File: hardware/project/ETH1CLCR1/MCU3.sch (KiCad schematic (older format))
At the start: 19 parts, among them J1201 Conn_02x05, U1001 STM32F413RGT6Tx, U1202 24LC08B-E/MS, Y1201 NX3225GD-8MHZ-STD-CRA-3

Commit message: Schematic design
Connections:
- net +3.3VP renamed +3.3VF
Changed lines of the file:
@@
 $Descr A3 16535 11693
 encoding utf-8
-Sheet 10 14
+Sheet 9 16
 Title ""
 Date ""
@@
 Wire Wire Line
 	7400 3100 7500 3100
-$Comp
-L power:+3.3VP #PWR?
-U 1 1 5E29D79D
-P 7550 3050
-AR Path="/5DF36C25/5E29D79D" Ref="#PWR?"  Part="1"
-AR Path="/5E29C232/5E29D79D" Ref="#PWR01201"  Part="1"
-AR Path="/5DF38F82/5E29D79D" Ref="#PWR01001"  Part="1"
-F 0 "#PWR01001" H 7700 3000 50  0001 C CNN
-F 1 "+3.3VP" H 7570 3193 50  0000 C CNN
-F 2 "" H 7550 3050 50  0001 C CNN
-F 3 "" H 7550 3050 50  0001 C CNN
-	1    7550 3050
-	1    0    0    -1
-$EndComp
 Wire Wire Line
 	7550 3050 7550 3100
@@
 Connection ~ 9300 9800
 $Comp
-L power:+3.3VP #PWR01010
-U 1 1 5E770710
-P 9900 10050
-F 0 "#PWR01010" H 10050 10000 50  0001 C CNN
-F 1 "+3.3VP" H 9920 10193 50  0000 C CNN
-F 2 "" H 9900 10050 50  0001 C CNN
-F 3 "" H 9900 10050 50  0001 C CNN
-	1    9900 10050
-	1    0    0    -1
-$EndComp
-$Comp
 L ETH1CLCR1:DGNDF #PWR01014
 U 1 1 5E77122F
@@
 	1    0    0    -1
 $EndComp
-$Comp
-L power:+3.3VP #PWR01009
-U 1 1 5E7718B5
-P 8000 9950
-F 0 "#PWR01009" H 8150 9900 50  0001 C CNN
-F 1 "+3.3VP" H 8020 10093 50  0000 C CNN
-F 2 "" H 8000 9950 50  0001 C CNN
-F 3 "" H 8000 9950 50  0001 C CNN
-	1    8000 9950
-	1    0    0    -1
-$EndComp
 Wire Wire Line
 	8000 9950 8000 10000
-$Comp
-L power:+3.3VP #PWR01008
-U 1 1 5E772DFA
-P 9300 9750
-F 0 "#PWR01008" H 9450 9700 50  0001 C CNN
-F 1 "+3.3VP" H 9320 9893 50  0000 C CNN
-F 2 "" H 9300 9750 50  0001 C CNN
-F 3 "" H 9300 9750 50  0001 C CNN
-	1    9300 9750
-	1    0    0    -1
-$EndComp
 $Comp
 L Device:C C1003
@@
 F 3 "" H 14150 6300 50  0001 C CNN
 	1    14150 6300
-	1    0    0    -1
-$EndComp
-$Comp
-L power:+3.3VP #PWR01002
-U 1 1 5E7C0507
-P 14150 5600
-F 0 "#PWR01002" H 14300 5550 50  0001 C CNN
-F 1 "+3.3VP" H 14170 5743 50  0000 C CNN
-F 2 "" H 14150 5600 50  0001 C CNN
-F 3 "" H 14150 5600 50  0001 C CNN
-	1    14150 5600
 	1    0    0    -1
 $EndComp
@@
 Wire Wire Line
 	2200 10700 2450 10700
-$Comp
-L power:+3.3VP #PWR01011
-U 1 1 5E10E793
-P 2200 10250
-F 0 "#PWR01011" H 2350 10200 50  0001 C CNN
-F 1 "+3.3VP" H 2220 10393 50  0000 C CNN
-F 2 "" H 2200 10250 50  0001 C CNN
-F 3 "" H 2200 10250 50  0001 C CNN
-	1    2200 10250
-	1    0    0    -1
-$EndComp
 Wire Wire Line
 	2200 10250 2200 10300
@@
 $EndComp
 $Comp
-L power:+3.3VP #PWR01012
-U 1 1 5DEC5CD8
-P 4100 10250
-F 0 "#PWR01012" H 4250 10200 50  0001 C CNN
-F 1 "+3.3VP" H 4120 10393 50  0000 C CNN
-F 2 "" H 4100 10250 50  0001 C CNN
-F 3 "" H 4100 10250 50  0001 C CNN
-	1    4100 10250
-	1    0    0    -1
-$EndComp
-$Comp
 L ETH1CLCR1:DGNDF #PWR01017
 U 1 1 5DEC5F6E
@@
 Wire Wire Line
 	1850 5650 1900 5650
+$Comp
+L ETH1CLCR1:+3.3VF #PWR0110
+U 1 1 5E94700D
+P 2200 10250
+F 0 "#PWR0110" H 2200 10100 50  0001 C CNN
+F 1 "+3.3VF" H 2215 10423 50  0000 C CNN
+F 2 "" H 2200 10250 50  0001 C CNN
+F 3 "" H 2200 10250 50  0001 C CNN
+	1    2200 10250
+	1    0    0    -1
+$EndComp
+$Comp
+L ETH1CLCR1:+3.3VF #PWR0111
+U 1 1 5E9476B2
+P 4100 10250
+F 0 "#PWR0111" H 4100 10100 50  0001 C CNN
+F 1 "+3.3VF" H 4115 10423 50  0000 C CNN
+F 2 "" H 4100 10250 50  0001 C CNN
+F 3 "" H 4100 10250 50  0001 C CNN
+	1    4100 10250
+	1    0    0    -1
+$EndComp
+$Comp
+L ETH1CLCR1:+3.3VF #PWR0112
+U 1 1 5E94791E
+P 8000 9950
+F 0 "#PWR0112" H 8000 9800 50  0001 C CNN
+F 1 "+3.3VF" H 8015 10123 50  0000 C CNN
+F 2 "" H 8000 9950 50  0001 C CNN
+F 3 "" H 8000 9950 50  0001 C CNN
+	1    8000 9950
+	1    0    0    -1
+$EndComp
+$Comp
+L ETH1CLCR1:+3.3VF #PWR0113
+U 1 1 5E949139
+P 9300 9750
+F 0 "#PWR0113" H 9300 9600 50  0001 C CNN
+F 1 "+3.3VF" H 9315 9923 50  0000 C CNN
+F 2 "" H 9300 9750 50  0001 C CNN
+F 3 "" H 9300 9750 50  0001 C CNN
+	1    9300 9750
+	1    0    0    -1
+$EndComp
+$Comp
+L ETH1CLCR1:+3.3VF #PWR0114
+U 1 1 5E9493FF
+P 9900 10050
+F 0 "#PWR0114" H 9900 9900 50  0001 C CNN
+F 1 "+3.3VF" H 9915 10223 50  0000 C CNN
+F 2 "" H 9900 10050 50  0001 C CNN
+F 3 "" H 9900 10050 50  0001 C CNN
+	1    9900 10050
+	1    0    0    -1
+$EndComp
+$Comp
+L ETH1CLCR1:+3.3VF #PWR0115
+U 1 1 5E9495AA
+P 14150 5600
+F 0 "#PWR0115" H 14150 5450 50  0001 C CNN
+F 1 "+3.3VF" H 14165 5773 50  0000 C CNN
+F 2 "" H 14150 5600 50  0001 C CNN
+F 3 "" H 14150 5600 50  0001 C CNN
+	1    14150 5600
+	1    0    0    -1
+$EndComp
+$Comp
+L ETH1CLCR1:+3.3VF #PWR0116
+U 1 1 5E94B0CB
+P 7550 3050
+F 0 "#PWR0116" H 7550 2900 50  0001 C CNN
+F 1 "+3.3VF" H 7565 3223 50  0000 C CNN
+F 2 "" H 7550 3050 50  0001 C CNN
+F 3 "" H 7550 3050 50  0001 C CNN
+	1    7550 3050
+	1    0    0    -1
+$EndComp
 $EndSCHEMATC

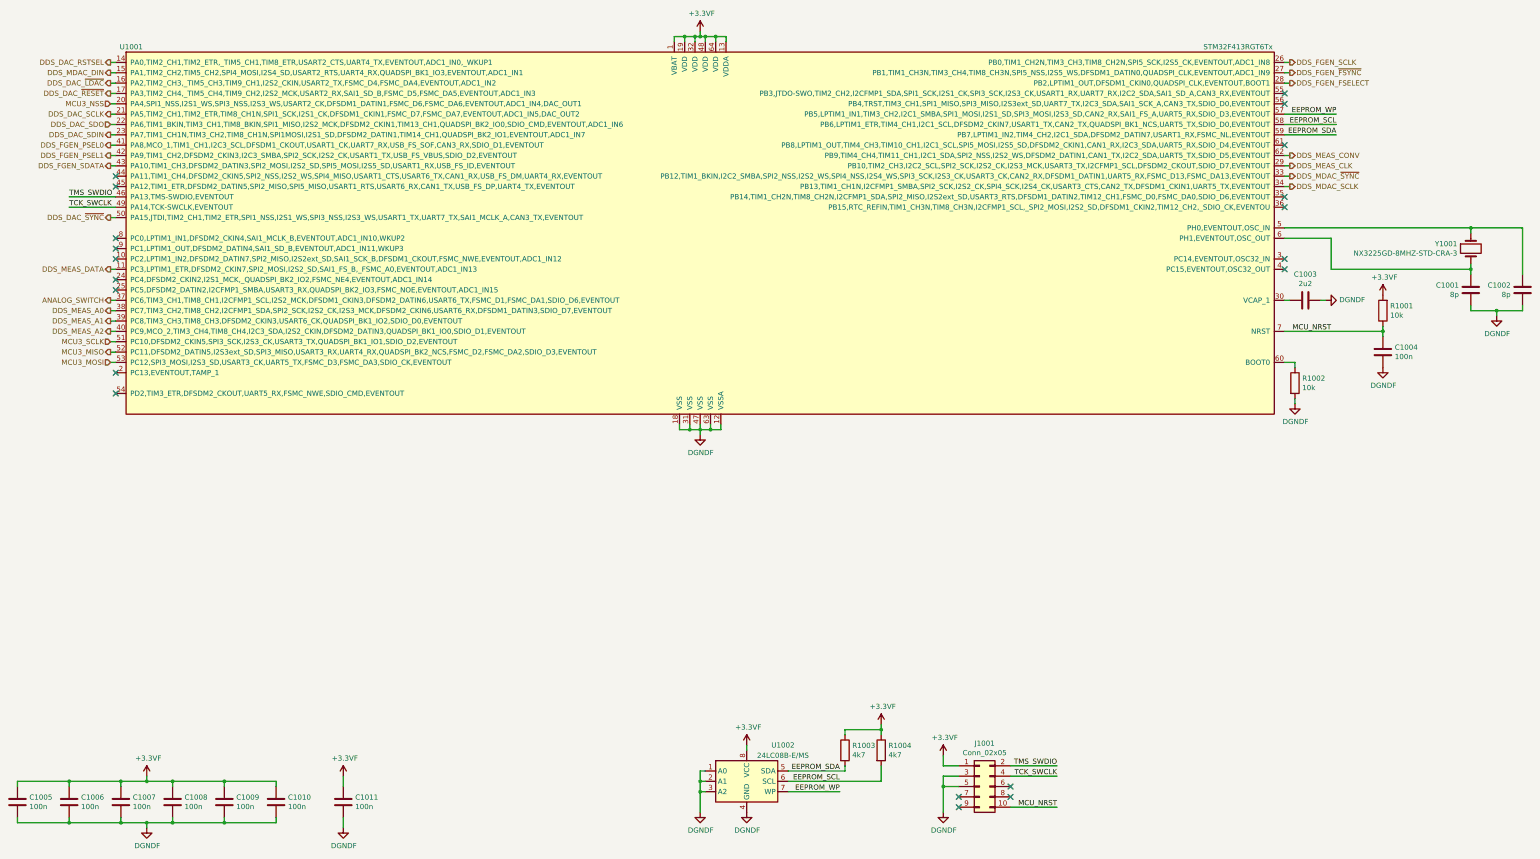
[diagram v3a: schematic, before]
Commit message: Footprint asigment (not finished).
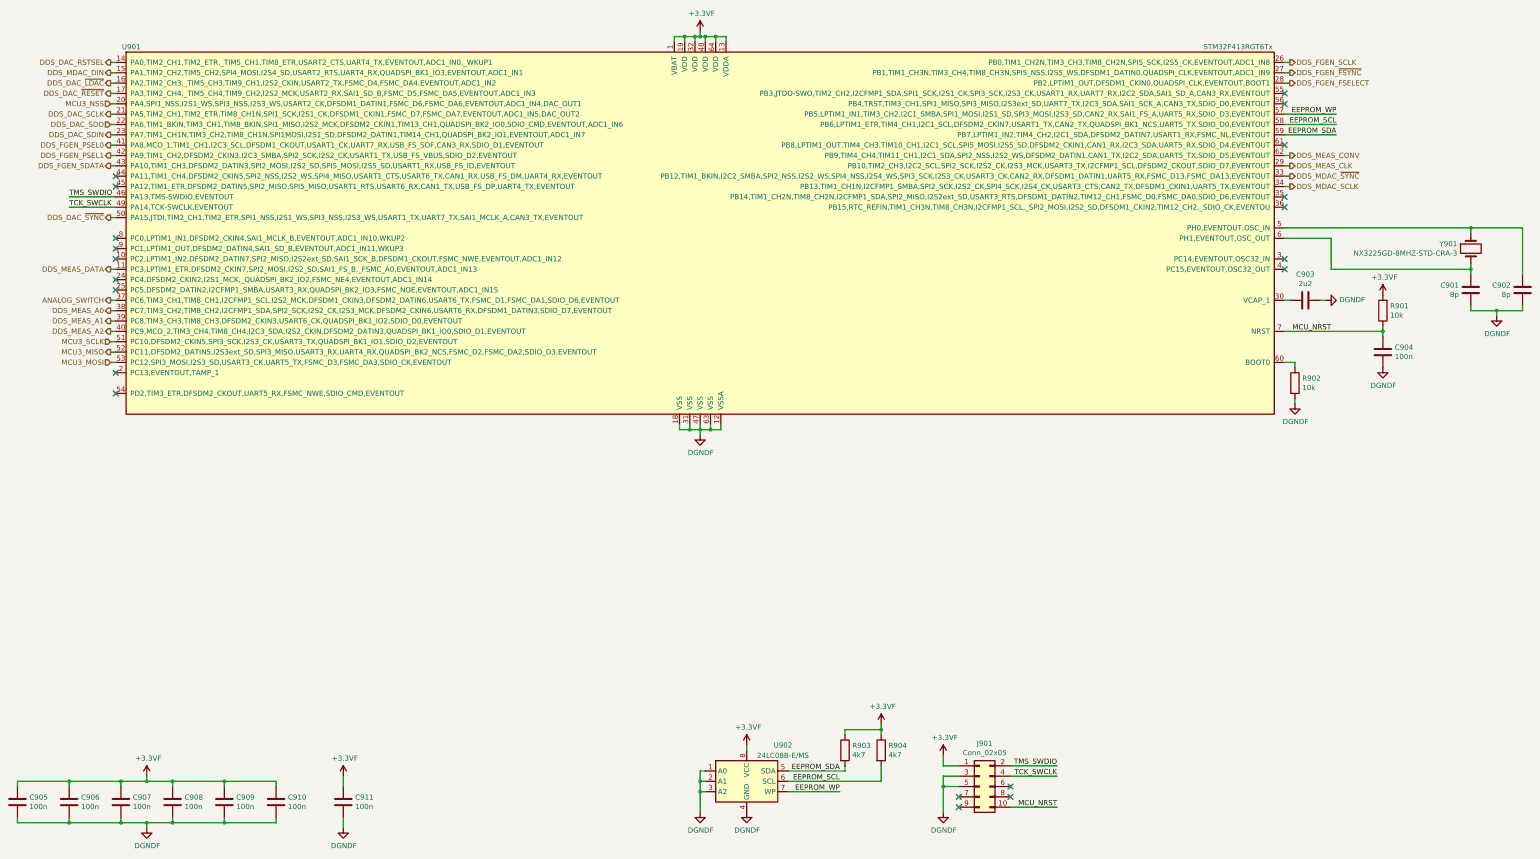
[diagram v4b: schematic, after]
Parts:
- renumbered C1201 to C901, C1202 to C902, C1003 to C903, C1004 to C904, C1005 to C905, C1006 to C906, C1007 to C907, C1008 to C908, C1009 to C909, C1010 to C910, C1011 to C911, J1201 to J901, R1001 to R901, R1202 to R902, R1203 to R903, R1204 to R904, U1001 to U901, U1202 to U902, Y1201 to Y901

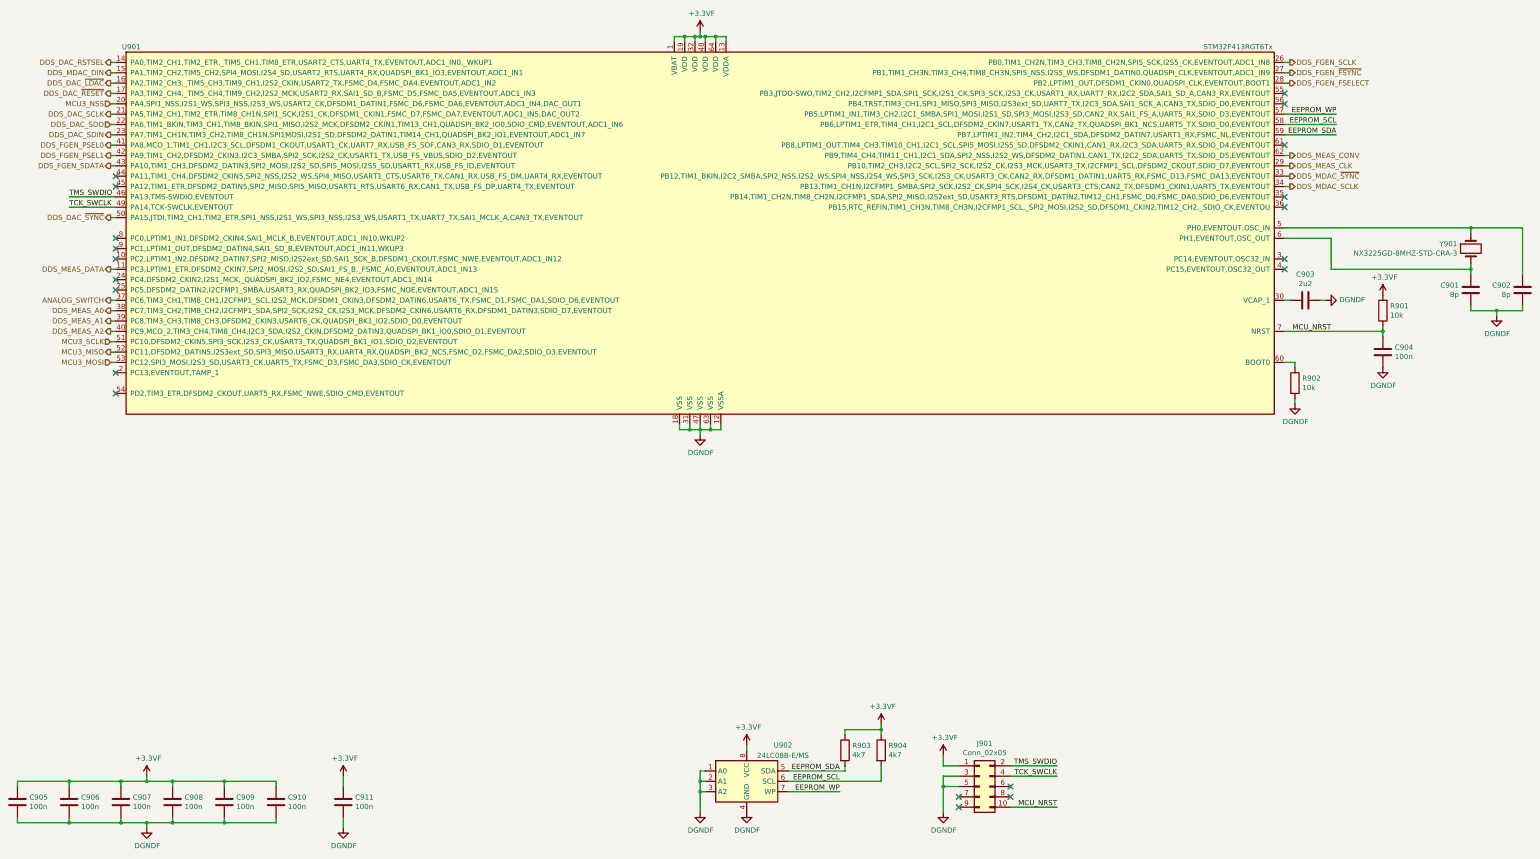
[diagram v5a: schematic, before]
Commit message: Redesinged ADC schematic.
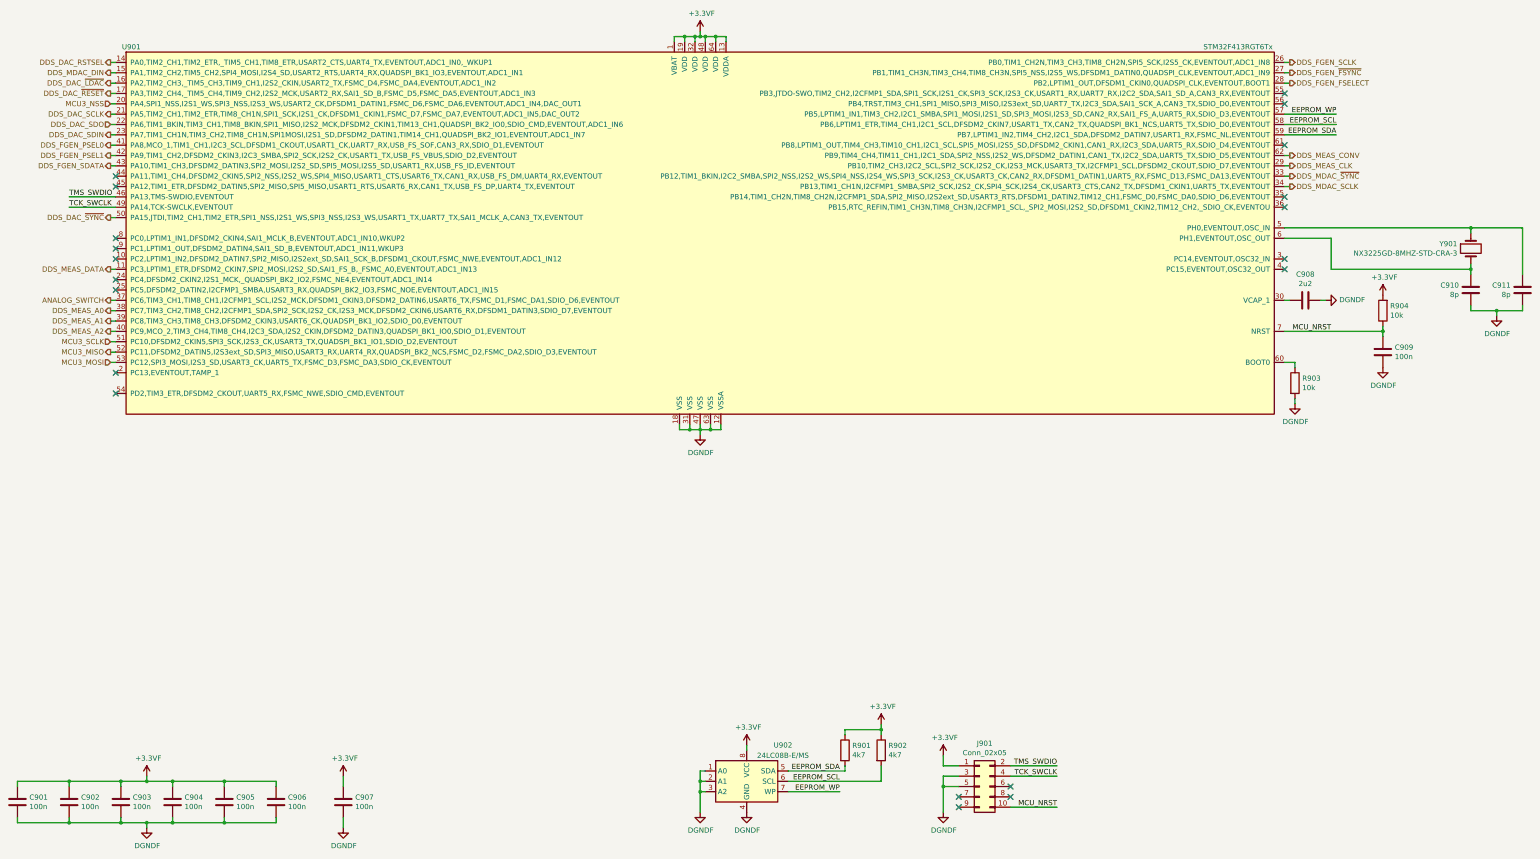
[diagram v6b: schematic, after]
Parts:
- renumbered C905 to C901, C906 to C902, C907 to C903, C908 to C904, C909 to C905, C910 to C906, C911 to C907, C903 to C908, C904 to C909, C901 to C910, C902 to C911, R903 to R901, R904 to R902, R902 to R903, R901 to R904

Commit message: Redesigned the power supply, added humidy+temp. sensor.
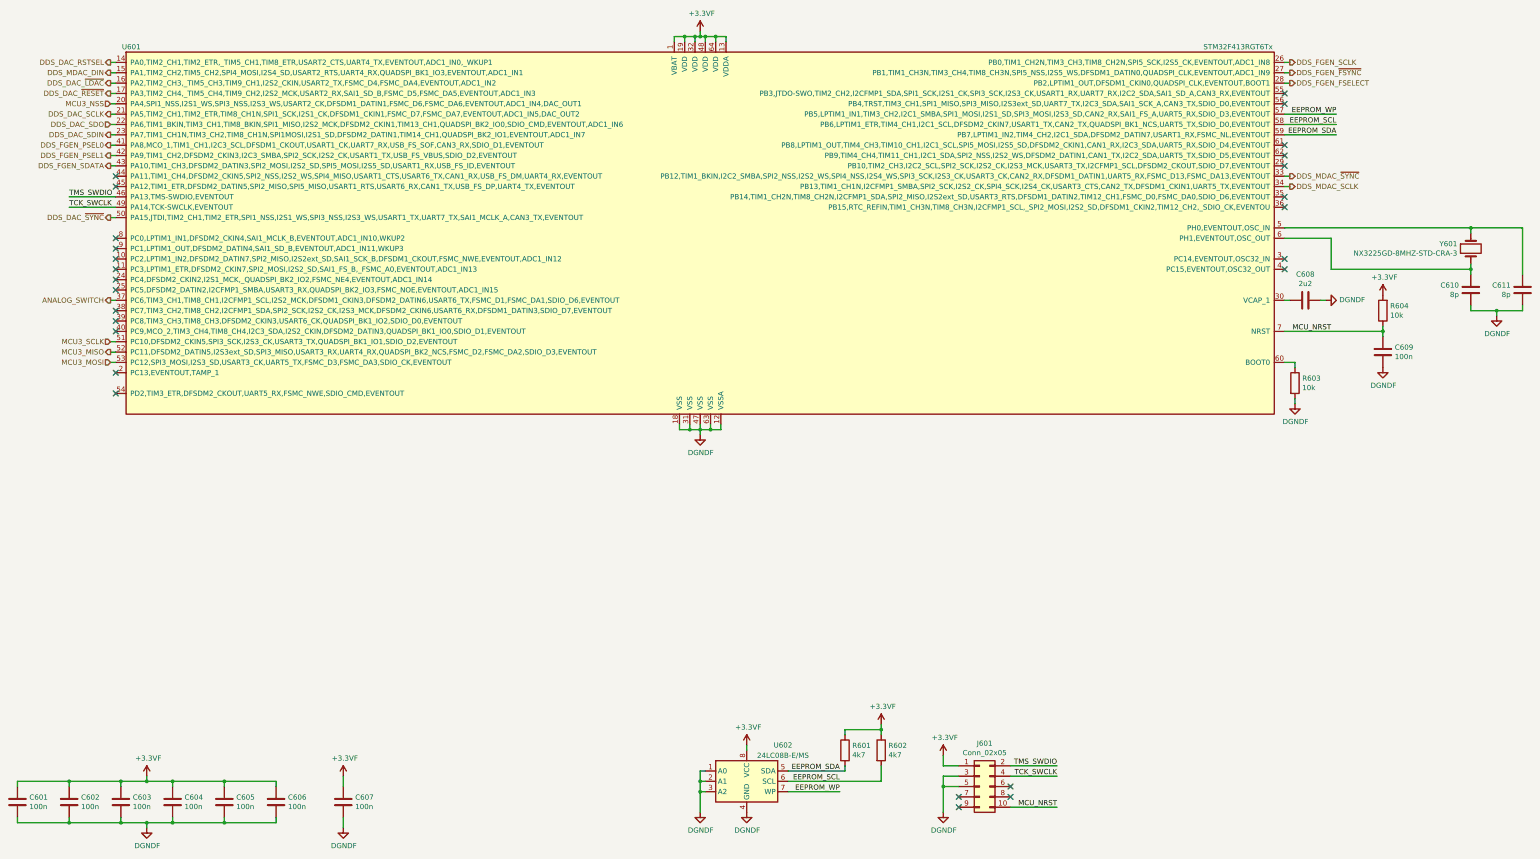
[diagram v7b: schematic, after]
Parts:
- renumbered C901 to C601, C902 to C602, C903 to C603, C904 to C604, C905 to C605, C906 to C606, C907 to C607, C908 to C608, C909 to C609, C910 to C610, C911 to C611, J901 to J601, R901 to R601, R902 to R602, R903 to R603, R904 to R604, U901 to U601, U902 to U602, Y901 to Y601
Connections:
- net DDS_MEAS_A0: no longer names the net of U601.38 (PC7,TIM3_CH2,TIM8_CH2,I2CFMP1_SDA,SPI2_SCK,I2S2_CK,I2S3_MCK,DFSDM2_CKIN6,USART6_RX,DFSDM1_DATIN3,SDIO_D7,EVENTOUT)
- net DDS_MEAS_A1: no longer names the net of U601.39 (PC8,TIM3_CH3,TIM8_CH3,DFSDM2_CKIN3,USART6_CK,QUADSPI_BK1_IO2,SDIO_D0,EVENTOUT)
- net DDS_MEAS_A2: no longer names the net of U601.40 (PC9,MCO_2,TIM3_CH4,TIM8_CH4,I2C3_SDA,I2S2_CKIN,DFSDM2_DATIN3,QUADSPI_BK1_IO0,SDIO_D1,EVENTOUT)
- net DDS_MEAS_CLK: no longer names the net of U601.29 (PB10,TIM2_CH3,I2C2_SCL,SPI2_SCK,I2S2_CK,I2S3_MCK,USART3_TX,I2CFMP1_SCL,DFSDM2_CKOUT,SDIO_D7,EVENTOUT)
- net DDS_MEAS_CONV: no longer names the net of U601.62 (PB9,TIM4_CH4,TIM11_CH1,I2C1_SDA,SPI2_NSS,I2S2_WS,DFSDM2_DATIN1,CAN1_TX,I2C2_SDA,UART5_TX,SDIO_D5,EVENTOUT)
- net DDS_MEAS_DATA: no longer names the net of U601.11 (PC3,LPTIM1_ETR,DFSDM2_CKIN7,SPI2_MOSI,I2S2_SD,SAI1_FS_B,_FSMC_A0,EVENTOUT,ADC1_IN13)
- no-connect marks 20 -> 26
